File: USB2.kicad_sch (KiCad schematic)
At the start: 44 parts, among them P1 USB_C_Plug_USB2.0, P2 USB_C_Plug_USB2.0, U2 TUSB2046BIVFR, U3 TPS2044BDR, U6 SN75240, U7 SN75240, Y1 MP060

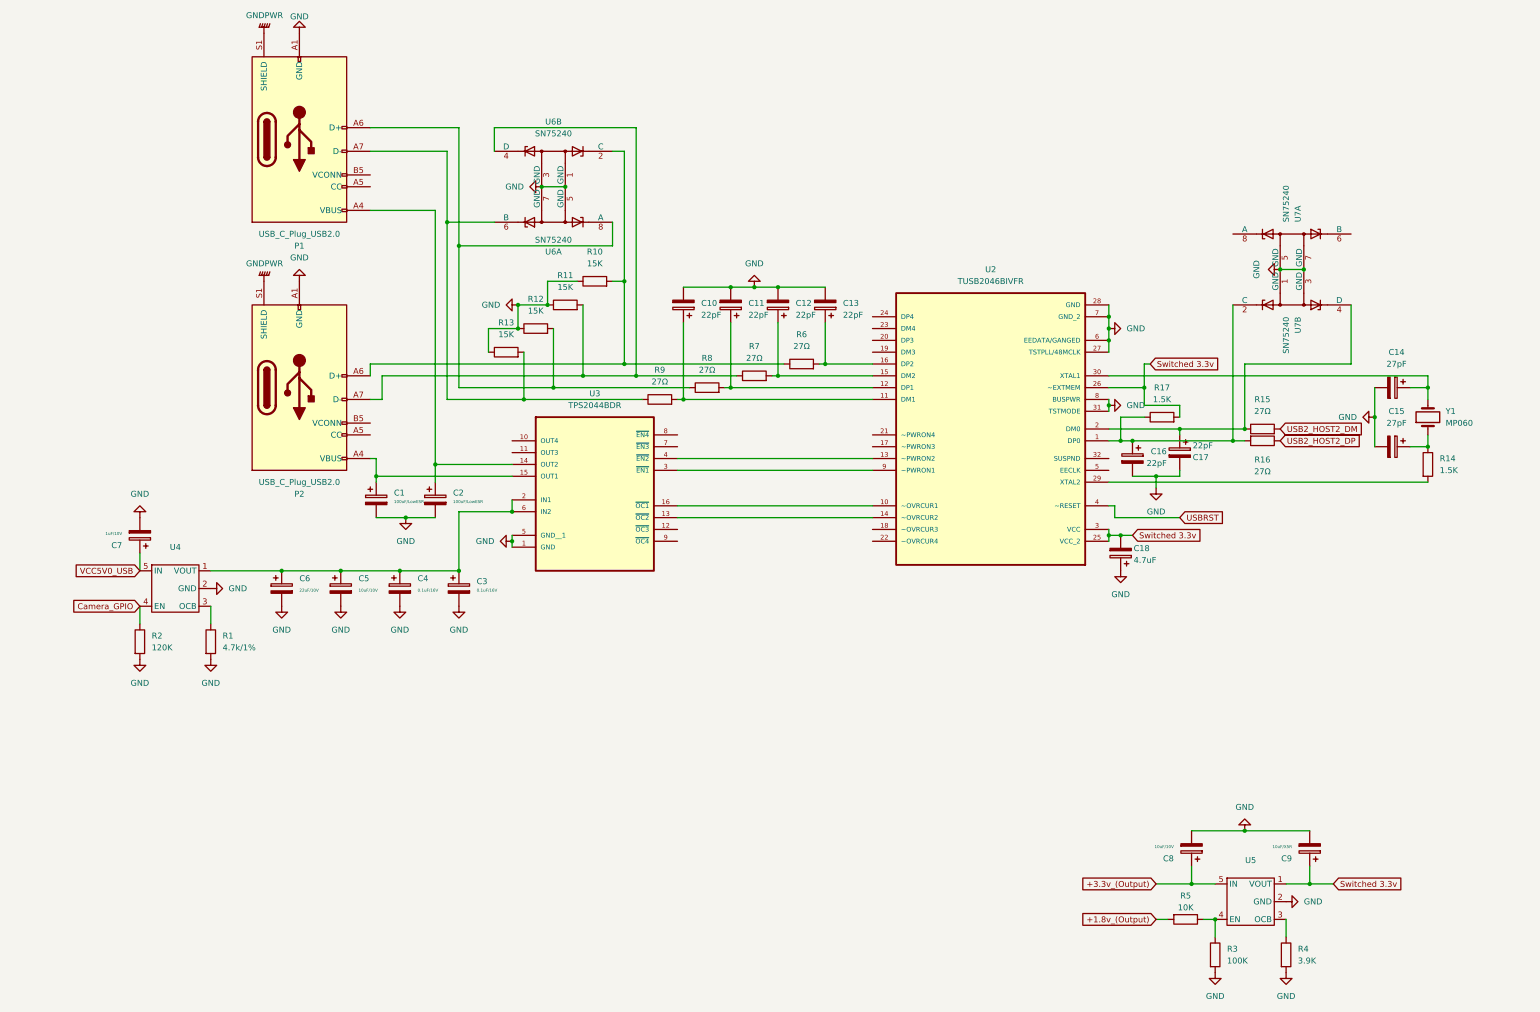
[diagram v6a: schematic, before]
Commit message: added power page
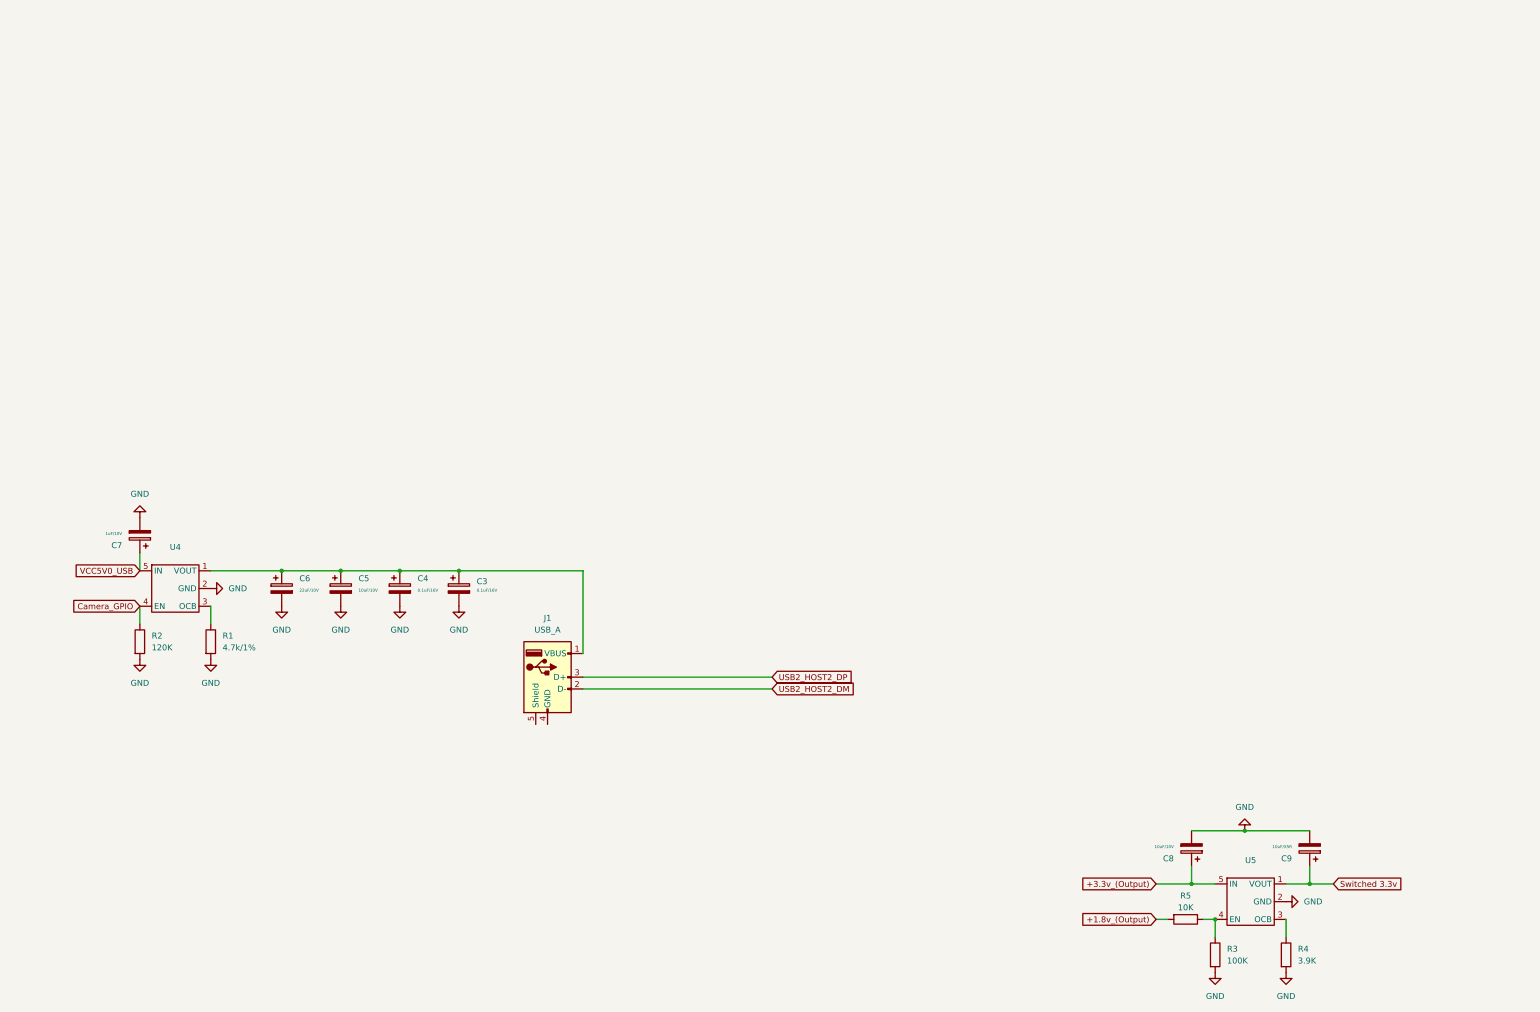
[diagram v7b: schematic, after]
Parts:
- removed C1, C2: 100uF/LowESR, symbol Device:C_Polarized
- removed C10, C11, C12, C13, C16, C17: 22pF, symbol Device:C_Polarized
- removed C14, C15: 27pF, symbol Device:C_Polarized
- removed C18: 4.7uF, symbol Device:C_Polarized
- removed P1, P2: USB_C_Plug_USB2.0, symbol Connector:USB_C_Plug_USB2.0
- removed R10, R11, R12, R13: 15K, symbol Device:R
- removed R14, R17: 1.5K, symbol Device:R
- removed R15, R16, R6, R7, R8, R9: 27Ω, symbol Device:R
- removed U2: TUSB2046BIVFR, TUSB2046BIVFR:QFP80P900X900X145-32N, symbol TUSB2046BIVFR:TUSB2046BIVFR
- removed U3: TPS2044BDR, TPS2044BDR:SOIC127P600X175-16N, symbol TPS2044BDR:TPS2044BDR
- removed U6, U7: SN75240, symbol Power_Protection:SN75240
- removed Y1: MP060, symbol Device:Crystal
- added J1: USB_A, symbol Connector:USB_A
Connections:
- net USB2_HOST2_DM: now also J1.2 (D-)
- net USB2_HOST2_DP: now also J1.3 (D+)
- net at C3.1, C4.1, C5.1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: now also J1.1 (VBUS)

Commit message: usb3 work cont
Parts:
- added D1, D2: ESD5311N-2/TR, Diode_SMD:Infineon_SG-WLL-2-3_0.58x0.28_P0.36mm, symbol Diode:ESD131-B1-W0201
- added FL1: MCZ1210AH900L2TD0G, symbol Filter:Choke_CommonMode_FerriteCore_1423
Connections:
- net GND: now also J1.4 (GND), D1.2 (A2), D2.2 (A2)
- net USB2_HOST2_DM: now also FL1.2; no longer J1.2 (D-)
- net USB2_HOST2_DP: now also FL1.1; no longer J1.3 (D+)
- net GNDPWR: now reaches J1.5 (Shield)
- new net: D1.1 (A1), FL1.4, J1.3 (D+)
- new net: D2.1 (A1), FL1.3, J1.2 (D-)
